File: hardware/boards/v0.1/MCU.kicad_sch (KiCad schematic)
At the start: 37 parts, among them J1 LOGIC, SW24 NRST, SW25 BOOT0, U1 BMDU, U18 STM32H743ZIT6, Y1 ECS-.327-12.5-1210-TR, Y4 8Q-25.000MEEV-T

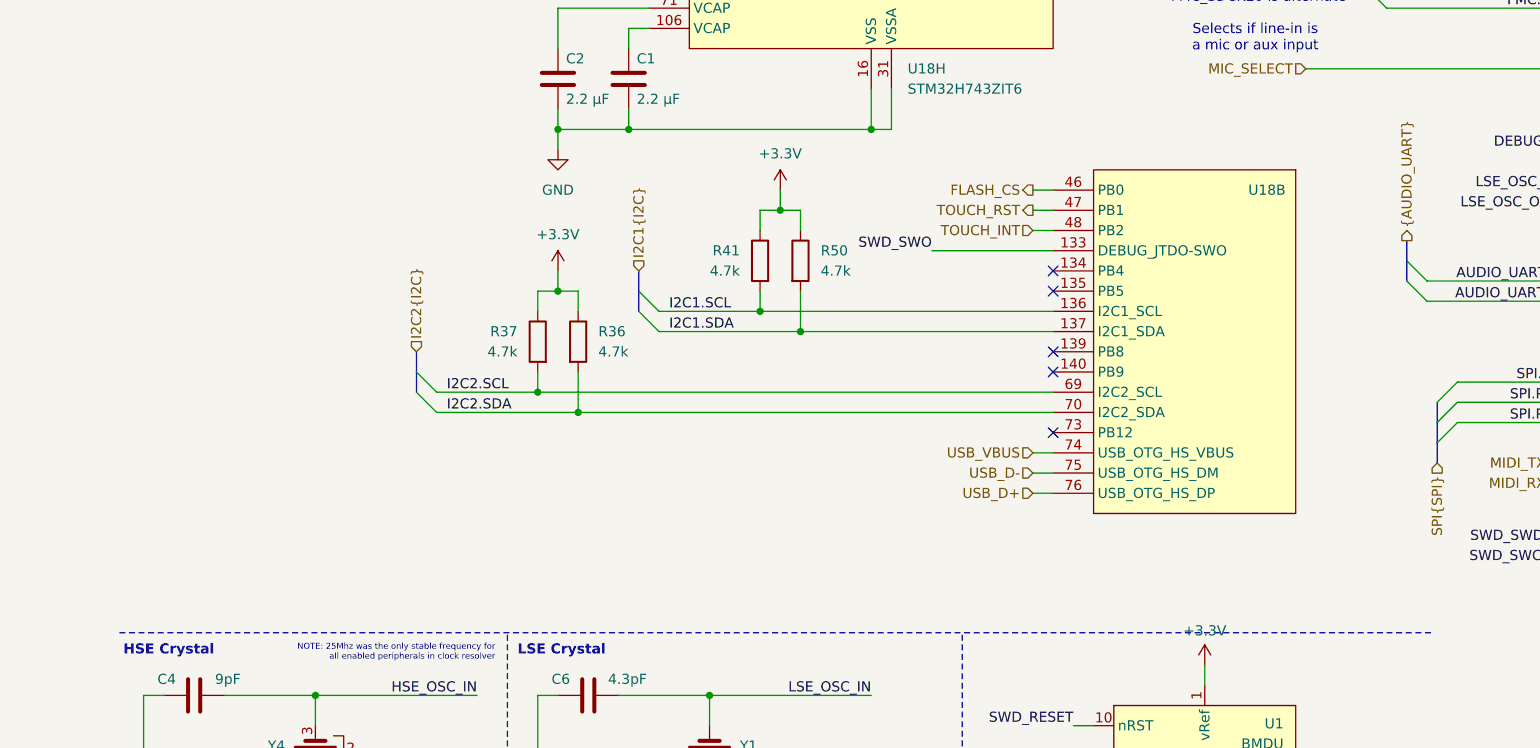
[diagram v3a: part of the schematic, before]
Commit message: feat: add touch screen connector, input I2C bus
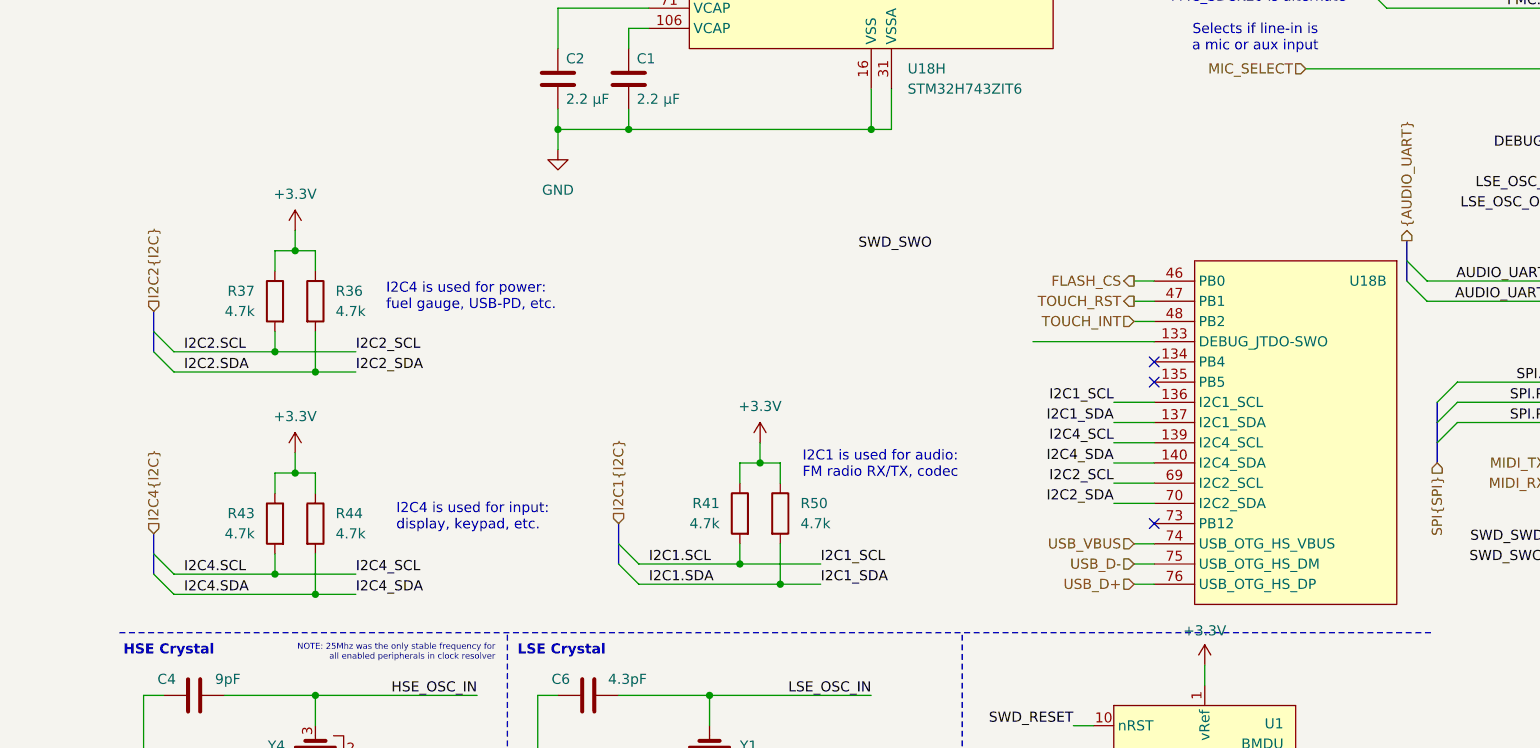
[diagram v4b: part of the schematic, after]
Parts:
- added R43, R44: 4.7k, Resistor_SMD:R_0402_1005Metric, symbol Device:R
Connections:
- net +3.3V: now also R43.1, R44.1
- net SWD_SWO: no longer U18.133 (PB3)
- net I2C4.SCL: now reaches U18.139 (PB8)
- net I2C4.SCL: now also R43.2
- net I2C4.SDA: now reaches U18.140 (PB9)
- net I2C4.SDA: now also R44.2
- no-connect marks 26 -> 24
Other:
- note added: "I2C1 is used for audio: FM radio RX/TX, codec"
- note added: "I2C4 is used for input: display, keypad, etc."
- note added: "I2C4 is used for power: fuel gauge, USB-PD, etc."
- moved on the sheet: R36, R37, R41, R50, U18B

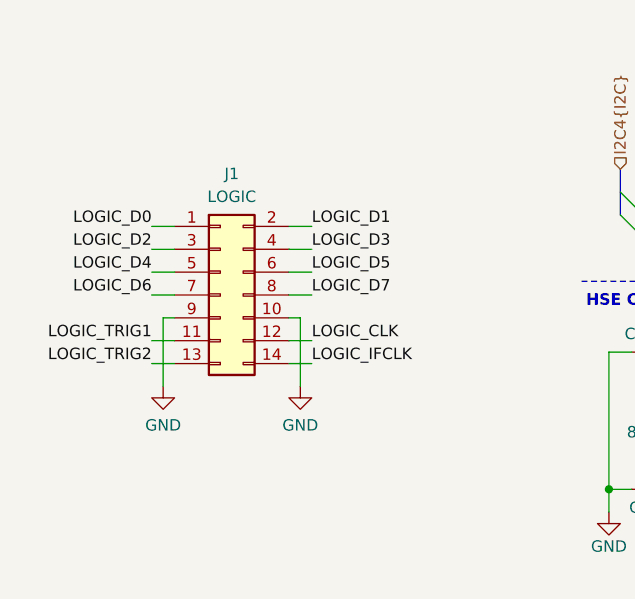
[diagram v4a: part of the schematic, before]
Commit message: feat: remove bitmagic connector
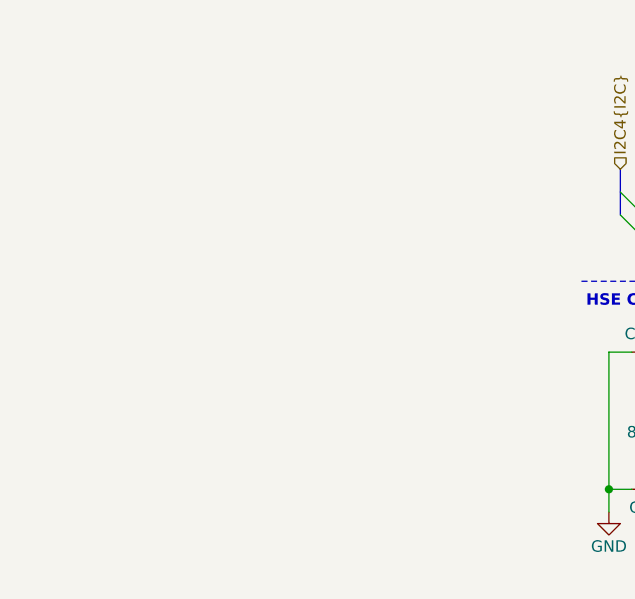
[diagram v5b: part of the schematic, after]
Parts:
- removed J1: LOGIC, pocket_synth:CON14_2X7_DUK_FTSH_SAI-M, symbol Connector_Generic:Conn_02x07_Odd_Even

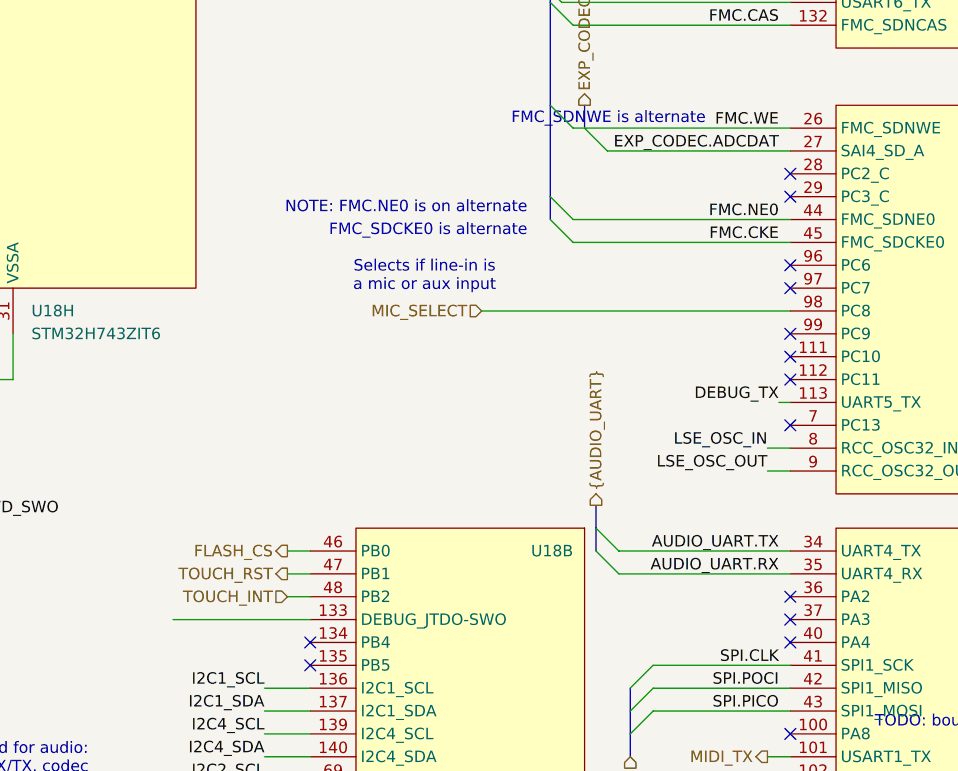
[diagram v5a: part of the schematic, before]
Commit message: feat: add IO expander for velocity pads
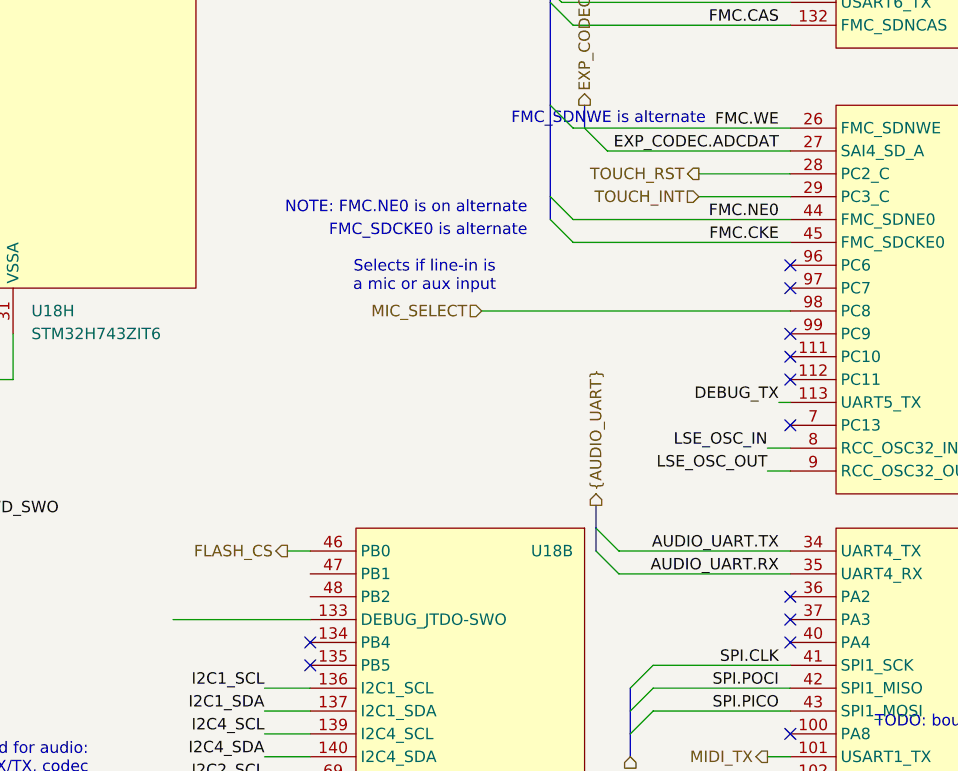
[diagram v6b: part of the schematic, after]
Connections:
- net TOUCH_INT: now also U18.29 (PC3_C); no longer U18.48 (PB2)
- net TOUCH_RST: now also U18.28 (PC2_C); no longer U18.47 (PB1)
- no-connect marks 24 -> 22
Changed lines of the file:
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@@
 	)
 	(no_connect
-		(at 195.58 80.01)
-	)
-	(no_connect
 		(at 195.58 55.88)
 	)
@@
 	)
 	(no_connect
-		(at 195.58 82.55)
-	)
-	(no_connect
 		(at 195.58 160.02)
 	)
@@
 	(wire
 		(pts
-			(xy 139.7 127) (xy 142.24 127)
+			(xy 185.42 82.55) (xy 195.58 82.55)
 		)
 		(stroke
@@
 	(wire
 		(pts
-			(xy 139.7 124.46) (xy 142.24 124.46)
+			(xy 185.42 80.01) (xy 195.58 80.01)
 		)
 		(stroke
@@
 	(hierarchical_label "TOUCH_INT"
 		(shape input)
-		(at 139.7 127 180)
+		(at 185.42 82.55 180)
 		(effects
 			(font
@@
 	(hierarchical_label "TOUCH_RST"
 		(shape output)
-		(at 139.7 124.46 180)
+		(at 185.42 80.01 180)
 		(effects
 			(font

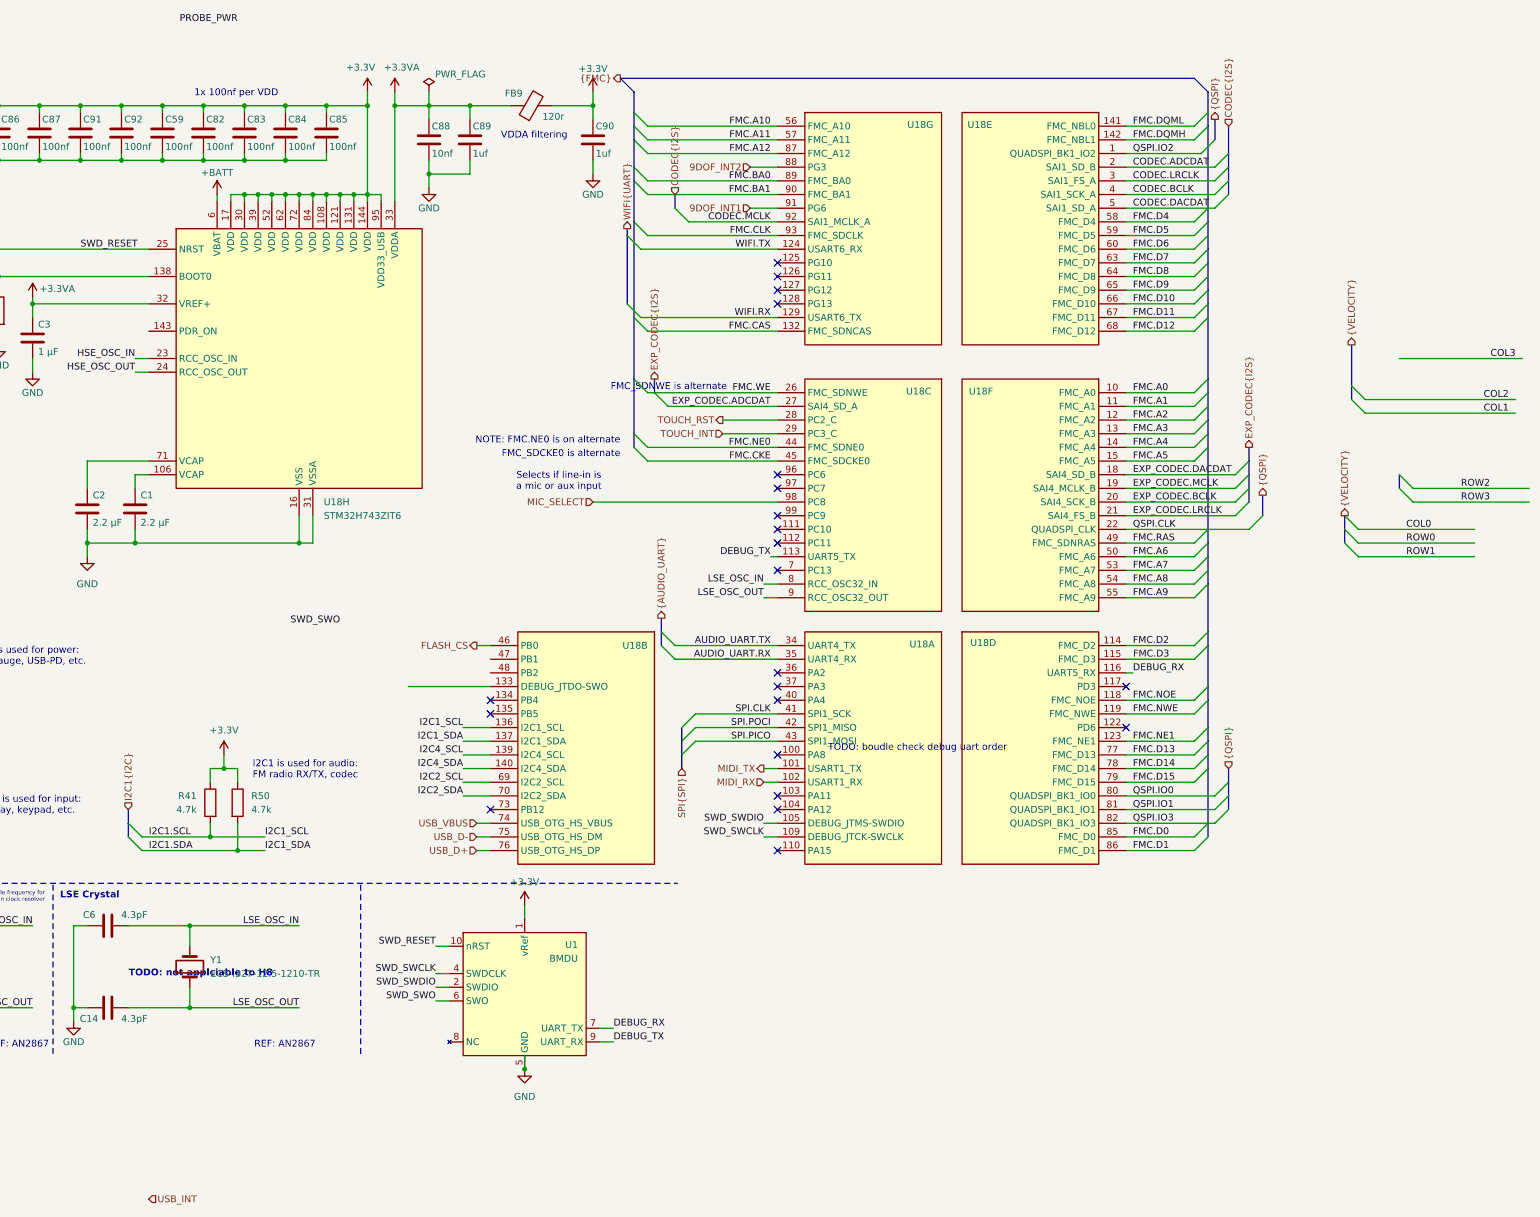
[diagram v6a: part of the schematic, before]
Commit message: feat: various ERC and DRC cleanup
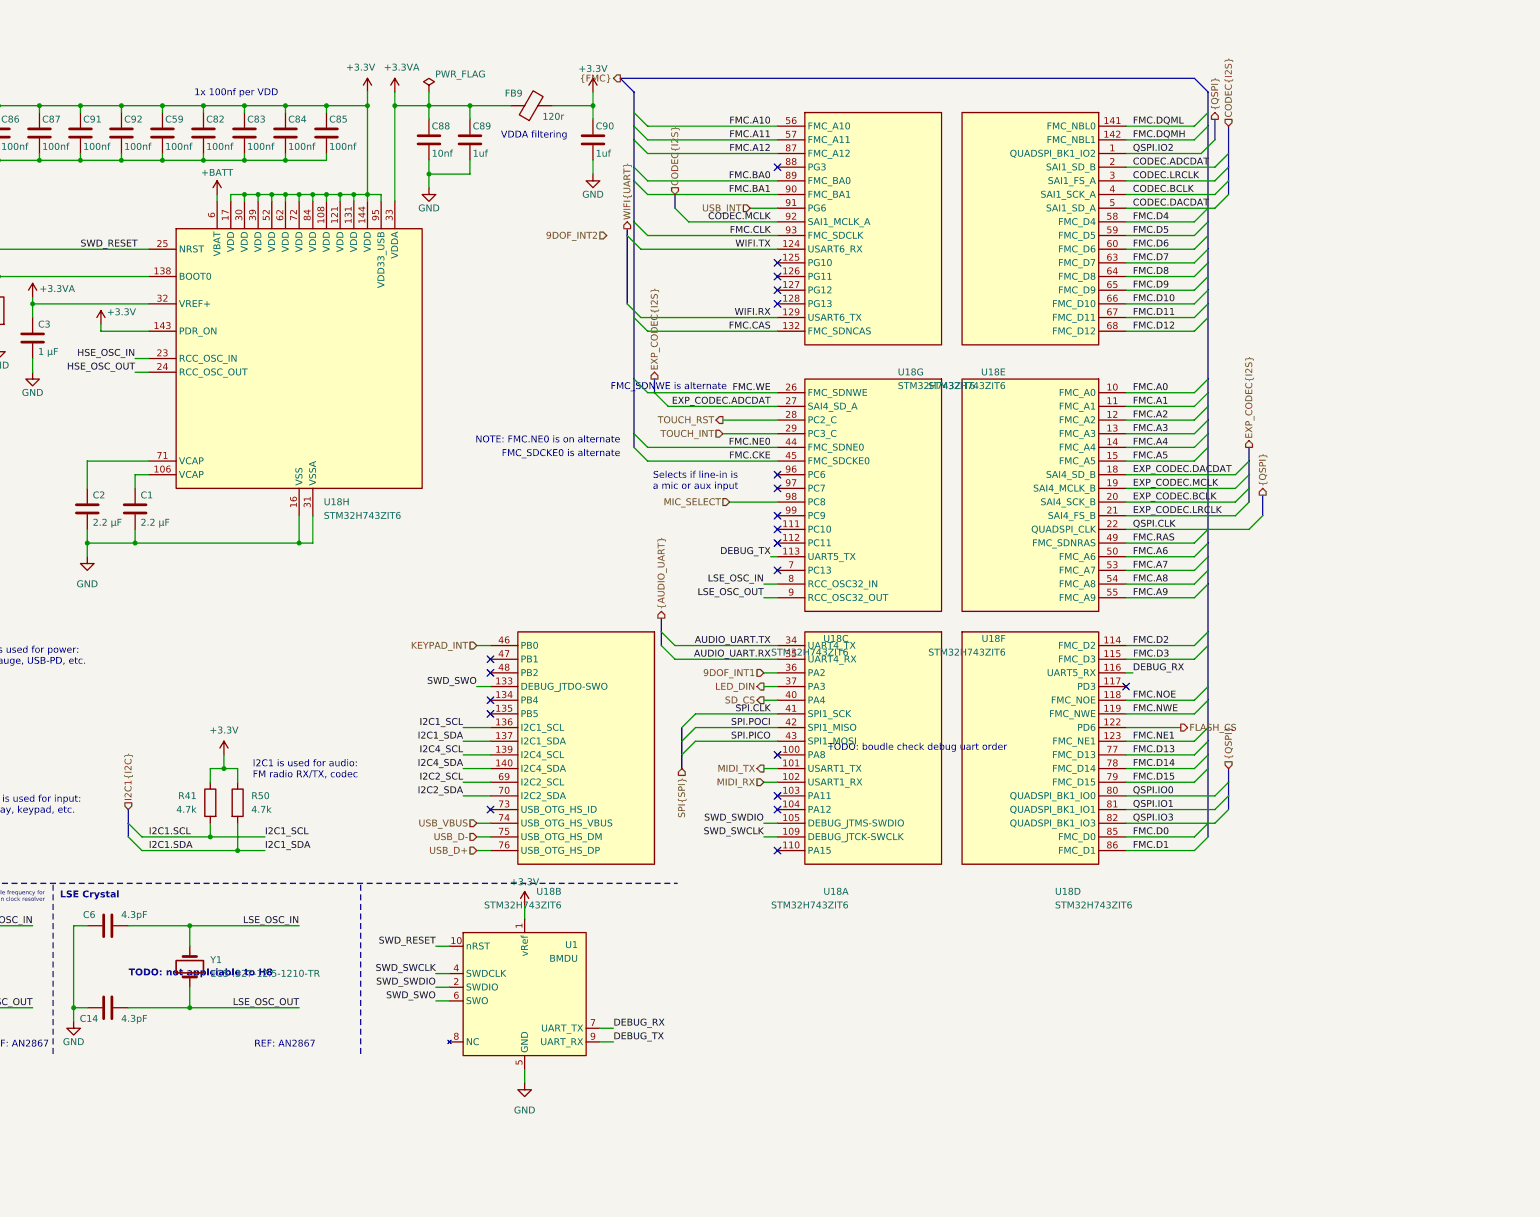
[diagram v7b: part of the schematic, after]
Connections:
- net +3.3V: now also U18.143 (PDR_ON)
- net 9DOF_INT1: now also U18.36 (PA2); no longer U18.91 (PG6)
- net 9DOF_INT2: no longer U18.88 (PG3)
- net FLASH_CS: now also U18.122 (PD6); no longer U18.46 (PB0)
- net SWD_SWO: now also U18.133 (PB3)
- net USB_INT: now also U18.91 (PG6)
- net LED_DIN: now reaches U18.37 (PA3)
- net SD_CS: now reaches U18.40 (PA4)
- new net KEYPAD_INT: U18.46 (PB0)
- no-connect marks 22 -> 21

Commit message: fix: incorrect symbol defined for MCU
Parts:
- U18: symbol MCU_ST_STM32H7:STM32H743ZITx -> pocket_synth:STM32H743ZITx
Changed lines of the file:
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@@
 	)
 	(symbol
-		(lib_name "STM32H743ZITx_5")
-		(lib_id "MCU_ST_STM32H7:STM32H743ZITx")
+		(lib_id "pocket_synth:STM32H743ZITx")
 		(at 213.36 140.97 0)
 		(mirror y)
@@
 	)
 	(symbol
-		(lib_name "STM32H743ZITx_7")
-		(lib_id "MCU_ST_STM32H7:STM32H743ZITx")
+		(lib_id "pocket_synth:STM32H743ZITx")
 		(at 242.57 140.97 0)
 		(unit 4)
@@
 	)
 	(symbol
-		(lib_name "STM32H743ZITx_1")
-		(lib_id "MCU_ST_STM32H7:STM32H743ZITx")
+		(lib_id "pocket_synth:STM32H743ZITx")
 		(at 242.57 44.45 0)
 		(mirror y)
@@
 	)
 	(symbol
-		(lib_name "STM32H743ZITx_6")
-		(lib_id "MCU_ST_STM32H7:STM32H743ZITx")
+		(lib_id "pocket_synth:STM32H743ZITx")
 		(at 242.57 93.98 0)
 		(mirror y)
@@
 	)
 	(symbol
-		(lib_name "STM32H743ZITx_3")
-		(lib_id "MCU_ST_STM32H7:STM32H743ZITx")
+		(lib_id "pocket_synth:STM32H743ZITx")
 		(at 213.36 93.98 0)
 		(mirror y)
@@
 	)
 	(symbol
-		(lib_name "STM32H743ZITx_2")
-		(lib_id "MCU_ST_STM32H7:STM32H743ZITx")
+		(lib_id "pocket_synth:STM32H743ZITx")
 		(at 213.36 44.45 0)
 		(unit 7)
@@
 	)
 	(symbol
-		(lib_name "STM32H743ZITx_4")
-		(lib_id "MCU_ST_STM32H7:STM32H743ZITx")
+		(lib_id "pocket_synth:STM32H743ZITx")
 		(at 160.02 140.97 0)
 		(mirror y)
